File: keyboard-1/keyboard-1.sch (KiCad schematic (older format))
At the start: 14 parts

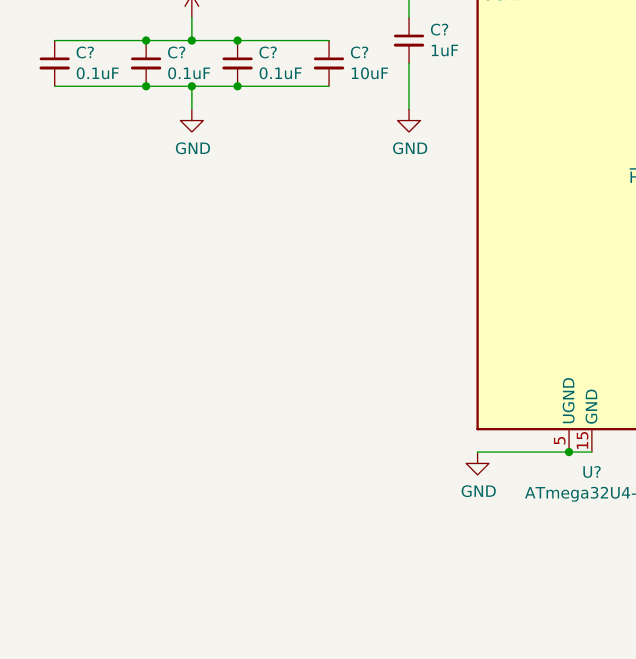
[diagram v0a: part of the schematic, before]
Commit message: mcu + usb-c connect
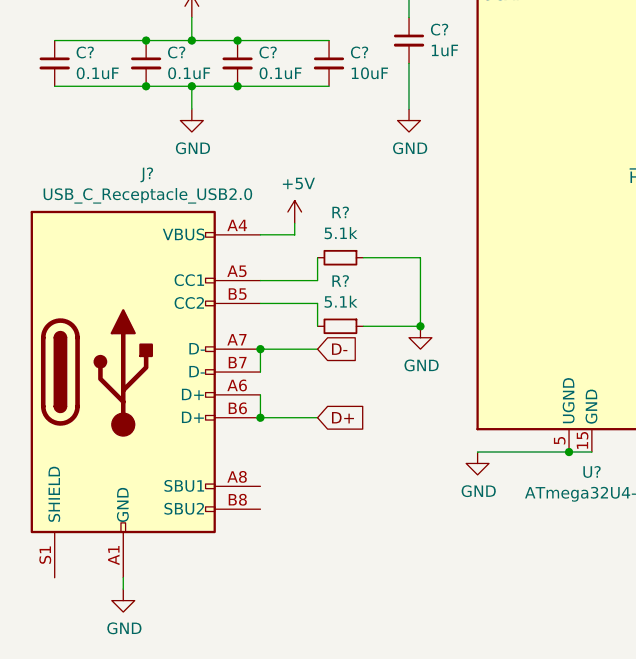
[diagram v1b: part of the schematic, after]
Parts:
- added J?: USB_C_Receptacle_USB2.0, symbol Connector:USB_C_Receptacle_USB2.0
- added R? (x2): 5.1k, symbol Device:R_Small
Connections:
- net +5V: now also J?.A4 (VBUS), J?.A9 (VBUS), J?.B4 (VBUS), J?.B9 (VBUS)
- net D+: now also J?.A6 (D+), J?.B6 (D+)
- net D-: now also J?.A7 (D-), J?.B7 (D-)
- net GND: now also J?.A1 (GND), J?.A12 (GND), J?.B1 (GND), J?.B12 (GND), R?.1, R?.1
- new net: J?.A5 (CC1), R?.2
- new net: J?.B5 (CC2), R?.2
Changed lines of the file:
@@
 Text GLabel 8350 3500 0    50   Input ~ 0
 D-
+$Comp
+L Connector:USB_C_Receptacle_USB2.0 J?
+U 1 1 601E80A6
+P 7750 5350
+F 0 "J?" H 7857 6217 50  0000 C CNN
+F 1 "USB_C_Receptacle_USB2.0" H 7857 6126 50  0000 C CNN
+F 2 "" H 7900 5350 50  0001 C CNN
+F 3 "https://www.usb.org/sites/default/files/documents/usb_type-c.zip" H 7900 5350 50  0001 C CNN
+	1    7750 5350
+	1    0    0    -1
+$EndComp
+$Comp
+L power:GND #PWR?
+U 1 1 601F3A88
+P 7750 6300
+F 0 "#PWR?" H 7750 6050 50  0001 C CNN
+F 1 "GND" H 7755 6127 50  0000 C CNN
+F 2 "" H 7750 6300 50  0001 C CNN
+F 3 "" H 7750 6300 50  0001 C CNN
+	1    7750 6300
+	1    0    0    -1
+$EndComp
+Wire Wire Line
+	7750 6250 7750 6300
+Text GLabel 8600 5550 2    50   Input ~ 0
+D+
+Text GLabel 8600 5250 2    50   Input ~ 0
+D-
+$Comp
+L power:+5V #PWR?
+U 1 1 601F53D3
+P 8500 4700
+F 0 "#PWR?" H 8500 4550 50  0001 C CNN
+F 1 "+5V" H 8515 4873 50  0000 C CNN
+F 2 "" H 8500 4700 50  0001 C CNN
+F 3 "" H 8500 4700 50  0001 C CNN
+	1    8500 4700
+	1    0    0    -1
+$EndComp
+Wire Wire Line
+	8350 4750 8500 4750
+Wire Wire Line
+	8500 4750 8500 4700
+Wire Wire Line
+	8350 5350 8350 5250
+Wire Wire Line
+	8350 5250 8600 5250
+Connection ~ 8350 5250
+Wire Wire Line
+	8350 5450 8350 5550
+Wire Wire Line
+	8350 5550 8600 5550
+Connection ~ 8350 5550
+$Comp
+L Device:R_Small R?
+U 1 1 601FA629
+P 8700 4850
+F 0 "R?" V 8504 4850 50  0000 C CNN
+F 1 "5.1k" V 8595 4850 50  0000 C CNN
+F 2 "" H 8700 4850 50  0001 C CNN
+F 3 "~" H 8700 4850 50  0001 C CNN
+	1    8700 4850
+	0    1    1    0
+$EndComp
+$Comp
+L Device:R_Small R?
+U 1 1 601FAF2C
+P 8700 5150
+F 0 "R?" V 8504 5150 50  0000 C CNN
+F 1 "5.1k" V 8595 5150 50  0000 C CNN
+F 2 "" H 8700 5150 50  0001 C CNN
+F 3 "~" H 8700 5150 50  0001 C CNN
+	1    8700 5150
+	0    1    1    0
+$EndComp
+$Comp
+L power:GND #PWR?
+U 1 1 601FB32C
+P 9050 5150
+F 0 "#PWR?" H 9050 4900 50  0001 C CNN
+F 1 "GND" H 9055 4977 50  0000 C CNN
+F 2 "" H 9050 5150 50  0001 C CNN
+F 3 "" H 9050 5150 50  0001 C CNN
+	1    9050 5150
+	1    0    0    -1
+$EndComp
+Wire Wire Line
+	8350 4950 8600 4950
+Wire Wire Line
+	8600 4950 8600 4850
+Wire Wire Line
+	8350 5050 8600 5050
+Wire Wire Line
+	8600 5050 8600 5150
+Wire Wire Line
+	8800 4850 9050 4850
+Wire Wire Line
+	9050 4850 9050 5150
+Wire Wire Line
+	8800 5150 9050 5150
+Connection ~ 9050 5150
 $EndSCHEMATC

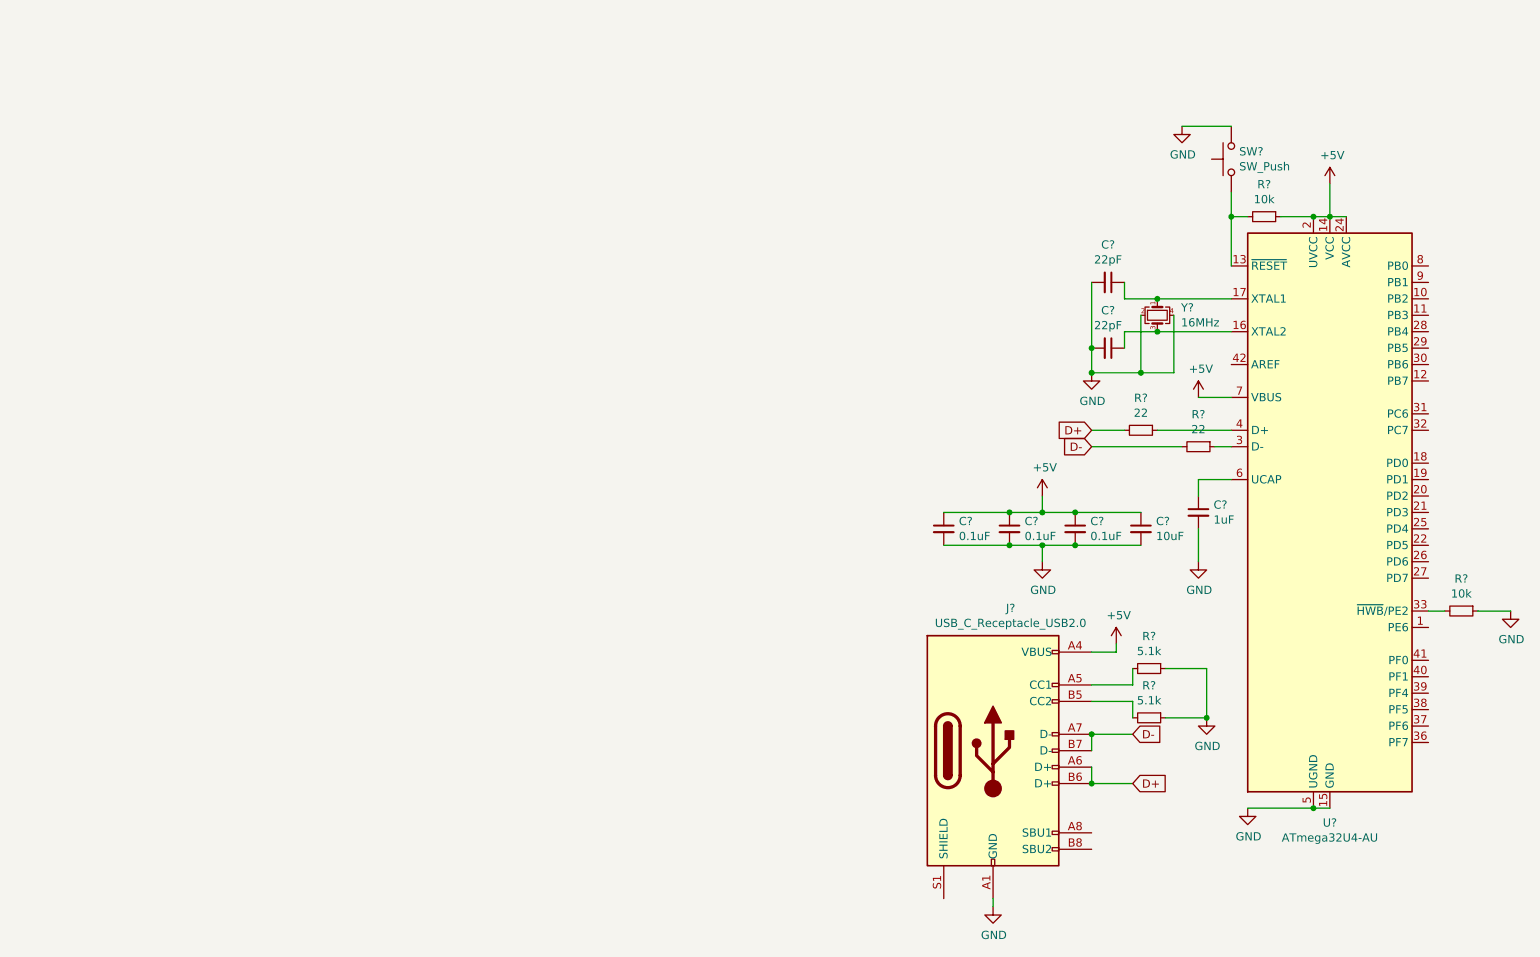
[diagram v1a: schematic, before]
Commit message: redo schematic, use double diodes, add column, use elite-c, start pcb design
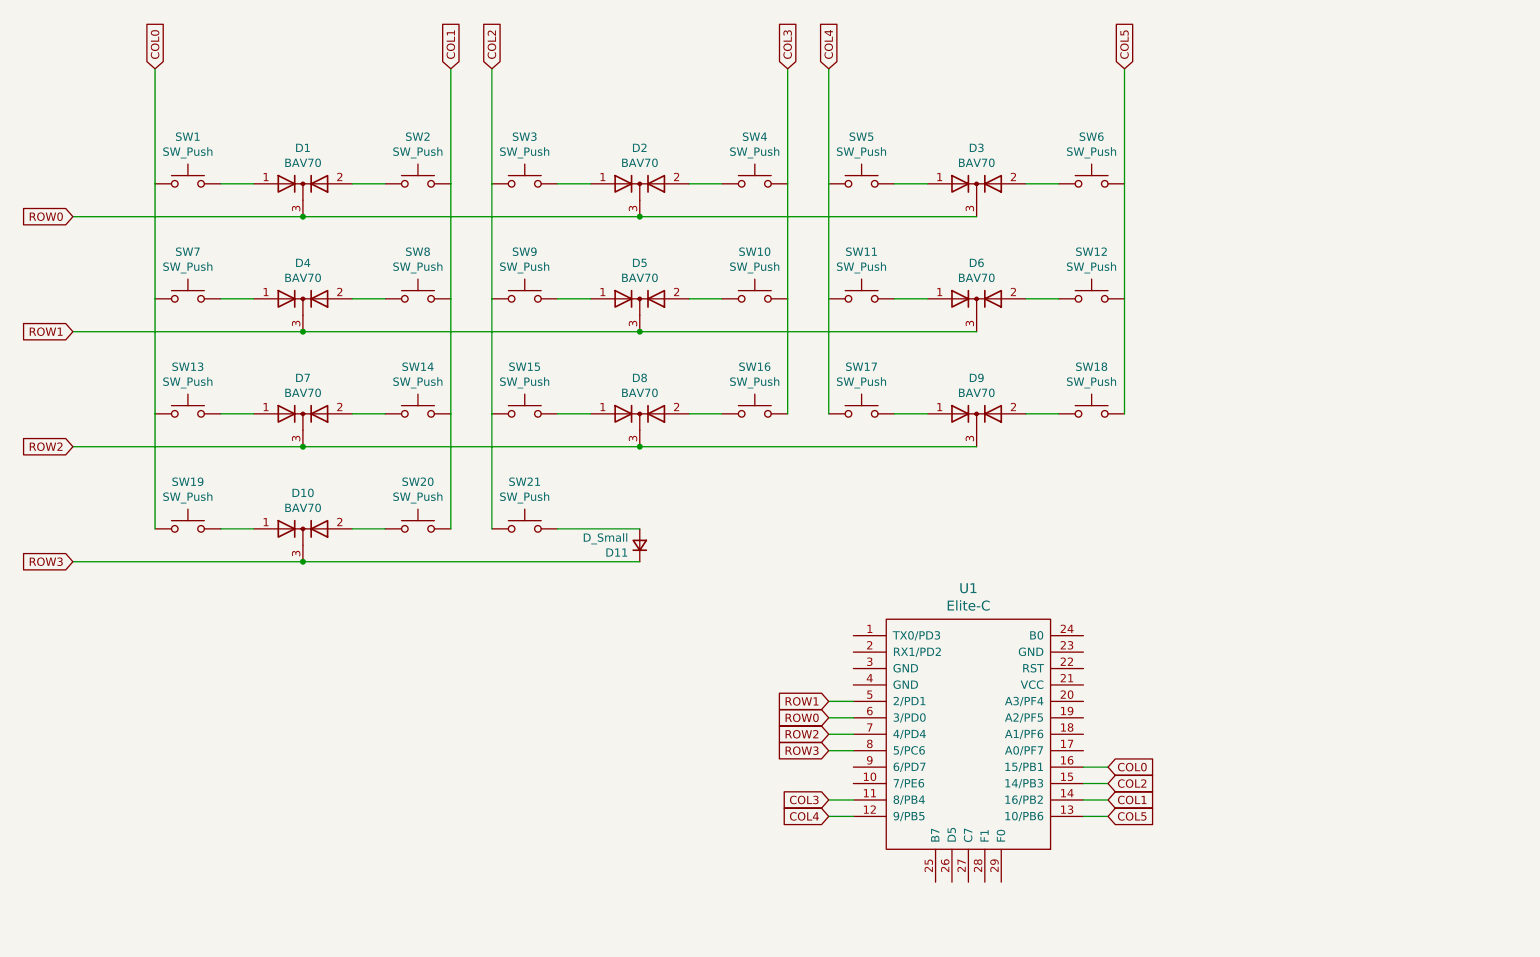
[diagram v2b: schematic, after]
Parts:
- removed C?: 1uF, symbol Device:C_Small
- removed C? (x3): 0.1uF, symbol Device:C_Small
- removed C?: 10uF, symbol Device:C_Small
- removed C? (x2): 22pF, symbol Device:C_Small
- removed J?: USB_C_Receptacle_USB2.0, symbol Connector:USB_C_Receptacle_USB2.0
- removed R? (x2): 10k, symbol Device:R_Small
- removed R? (x2): 22, symbol Device:R_Small
- removed R? (x2): 5.1k, symbol Device:R_Small
- removed SW?: SW_Push, symbol Switch:SW_Push
- removed U?: ATmega32U4-AU, Package_QFP:TQFP-44_10x10mm_P0.8mm, symbol MCU_Microchip_ATmega:ATmega32U4-AU
- removed Y?: 16MHz, symbol Device:Crystal_GND24_Small
- added D1, D10, D2, D3, D4, D5, D6, D7, D8, D9: BAV70, Package_TO_SOT_SMD:SOT-23, symbol Diode:BAV70
- added D11: D_Small, Diode_SMD:D_SOD-123, symbol Device:D_Small
- added SW1, SW10, SW11, SW12, SW13, SW14, SW15, SW16, SW17, SW18, SW19, SW2, SW20, SW21, SW3, SW4, SW5, SW6, SW7, SW8, SW9: SW_Push, Keebio-Parts:MX-Alps-Choc-1U, symbol Switch:SW_Push
- added U1: Elite-C, Keebio-Parts:Elite-C, symbol keebio:Elite-C
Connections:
- new net: D1.1 (A), SW1.2
- new net: D1.2 (A), SW2.1
- new net: D2.1 (A), SW3.2
- new net: D2.2 (A), SW4.1
- new net: D3.1 (A), SW5.2
- new net: D3.2 (A), SW6.1
- new net: D4.1 (A), SW7.2
- new net: D4.2 (A), SW8.1
- new net: D5.1 (A), SW9.2
- new net: D5.2 (A), SW10.1
- new net: D6.1 (A), SW11.2
- new net: D6.2 (A), SW12.1
- new net: D7.1 (A), SW13.2
- new net: D7.2 (A), SW14.1
- new net: D8.1 (A), SW15.2
- new net: D8.2 (A), SW16.1
- new net: D9.1 (A), SW17.2
- new net: D9.2 (A), SW18.1
- new net: D10.1 (A), SW19.2
- new net: D10.2 (A), SW20.1
- new net: D11.2 (A), SW21.2
- new net COL0: SW1.1, SW13.1, SW19.1, SW7.1, U1.16 (15/PB1)
- new net COL1: SW14.2, SW2.2, SW20.2, SW8.2, U1.14 (16/PB2)
- new net COL2: SW15.1, SW21.1, SW3.1, SW9.1, U1.15 (14/PB3)
- new net COL3: SW10.2, SW16.2, SW4.2, U1.11 (8/PB4)
- new net COL4: SW11.1, SW17.1, SW5.1, U1.12 (9/PB5)
- new net COL5: SW12.2, SW18.2, SW6.2, U1.13 (10/PB6)
- new net ROW0: D1.3 (K), D2.3 (K), D3.3 (K), U1.6 (3/PD0)
- new net ROW1: D4.3 (K), D5.3 (K), D6.3 (K), U1.5 (2/PD1)
- new net ROW2: D7.3 (K), D8.3 (K), D9.3 (K), U1.7 (4/PD4)
- new net ROW3: D10.3 (K), D11.1 (K), U1.8 (5/PC6)

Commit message: use generic connectors for elite C and add oled connectors, also add trrs connector
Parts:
- removed U1: Elite-C, Keebio-Parts:Elite-C, symbol keebio:Elite-C
- added J? (x2): Conn_01x12, symbol Connector_Generic:Conn_01x12
- added J?: Conn_01x04_Female, Connector_PinSocket_2.54mm:PinSocket_1x01_P2.54mm_Vertical, symbol Connector:Conn_01x04_Female
- added U2: TRRS, Keebio-Parts:TRRS-PJ-320A, symbol keebio:TRRS
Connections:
- net COL0: now also J?.4 (Pin_4)
- net COL1: now also J?.2 (Pin_2)
- net COL2: now also J?.3 (Pin_3)
- net COL3: now also J?.11 (Pin_11)
- net COL4: now also J?.12 (Pin_12)
- net COL5: now also J?.1 (Pin_1)
- net ROW0: now also J?.8 (Pin_8)
- net ROW1: now also J?.7 (Pin_7)
- net ROW2: now also J?.6 (Pin_6)
- net ROW3: now also J?.5 (Pin_5)
- new net GND: J?.11 (Pin_11), J?.4 (Pin_4), U2.1 (SLEEVE)
- new net SCL: J?.2 (Pin_2), J?.6 (Pin_6)
- new net SDA: J?.1 (Pin_1), J?.5 (Pin_5)
- new net SERIAL: J?.2 (Pin_2), U2.4 (RING2)
- new net VCC: J?.3 (Pin_3), J?.9 (Pin_9), U2.2 (TIP)
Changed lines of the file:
@@
 $EndDescr
-$Comp
-L keebio:Elite-C U1
-U 1 1 602DAF31
-P 7600 5200
-F 0 "U1" H 7600 6037 60  0000 C CNN
-F 1 "Elite-C" H 7600 5931 60  0000 C CNN
-F 2 "Keebio-Parts:Elite-C" V 8650 2700 60  0001 C CNN
-F 3 "" V 8650 2700 60  0001 C CNN
-	1    7600 5200
-	1    0    0    -1
-$EndComp
-Text GLabel 6750 1200 1    50   Input ~ 0
-COL4
-Text GLabel 6500 1200 1    50   Input ~ 0
-COL3
-Text GLabel 4700 1200 1    50   Input ~ 0
-COL2
-Text GLabel 4450 1200 1    50   Input ~ 0
-COL1
-Text GLabel 2650 1200 1    50   Input ~ 0
-COL0
-Text GLabel 6750 5350 0    50   Input ~ 0
-ROW3
-Text GLabel 2150 3500 0    50   Input ~ 0
-ROW2
-Text GLabel 2150 2800 0    50   Input ~ 0
-ROW1
-Text GLabel 2150 2100 0    50   Input ~ 0
-ROW0
 $Comp
 L Switch:SW_Push SW1
@@
 Wire Wire Line
 	7950 1900 8150 1900
-Text GLabel 8550 1200 1    50   Input ~ 0
-COL5
 Wire Wire Line
 	2150 2100 3550 2100
@@
 Wire Wire Line
 	5600 4000 5100 4000
-Text GLabel 6750 5150 0    50   Input ~ 0
+$Comp
+L keebio:TRRS U2
+U 1 1 603D1957
+P 5150 5300
+F 0 "U2" H 5067 5113 60  0000 C CNN
+F 1 "TRRS" H 5067 5219 60  0000 C CNN
+F 2 "Keebio-Parts:TRRS-PJ-320A" H 5300 5300 60  0001 C CNN
+F 3 "" H 5300 5300 60  0001 C CNN
+	1    5150 5300
+	-1   0    0    1
+$EndComp
+$Comp
+L power:VCC #PWR0103
+U 1 1 60418EEF
+P 5400 6000
+F 0 "#PWR0103" H 5400 5850 50  0001 C CNN
+F 1 "VCC" H 5415 6173 50  0000 C CNN
+F 2 "" H 5400 6000 50  0001 C CNN
+F 3 "" H 5400 6000 50  0001 C CNN
+	1    5400 6000
+	1    0    0    -1
+$EndComp
+$Comp
+L power:GND #PWR0104
+U 1 1 6041933E
+P 5650 5200
+F 0 "#PWR0104" H 5650 4950 50  0001 C CNN
+F 1 "GND" H 5655 5027 50  0000 C CNN
+F 2 "" H 5650 5200 50  0001 C CNN
+F 3 "" H 5650 5200 50  0001 C CNN
+	1    5650 5200
+	1    0    0    -1
+$EndComp
+Wire Wire Line
+	5500 5400 5500 5200
+Wire Wire Line
+	5500 5200 5650 5200
+Wire Wire Line
+	5500 5700 5500 6000
+Wire Wire Line
+	5500 6000 5400 6000
+$Comp
+L Connector_Generic:Conn_01x12 J?
+U 1 1 6044E7FE
+P 2450 5950
+F 0 "J?" H 2530 5942 50  0000 L CNN
+F 1 "Conn_01x12" H 2530 5851 50  0000 L CNN
+F 2 "" H 2450 5950 50  0001 C CNN
+F 3 "~" H 2450 5950 50  0001 C CNN
+	1    2450 5950
+	1    0    0    -1
+$EndComp
+$Comp
+L Connector_Generic:Conn_01x12 J?
+U 1 1 60456305
+P 3250 6050
+F 0 "J?" H 3168 5225 50  0000 C CNN
+F 1 "Conn_01x12" H 3168 5316 50  0000 C CNN
+F 2 "" H 3250 6050 50  0001 C CNN
+F 3 "~" H 3250 6050 50  0001 C CNN
+	1    3250 6050
+	-1   0    0    1
+$EndComp
+Wire Wire Line
+	3450 6050 3600 6050
+Wire Wire Line
+	3600 6150 3450 6150
+Wire Wire Line
+	3450 6250 3600 6250
+Wire Wire Line
+	3600 6350 3450 6350
+Wire Wire Line
+	3450 6450 3600 6450
+Wire Wire Line
+	3450 6550 3600 6550
+Wire Wire Line
+	3450 5850 3600 5850
+Wire Wire Line
+	3600 5950 3450 5950
+$Comp
+L Connector:Conn_01x04_Female J?
+U 1 1 60477B7D
+P 5350 7400
+F 0 "J?" V 5196 7548 50  0000 L CNN
+F 1 "Conn_01x04_Female" V 5287 7548 50  0000 L CNN
+F 2 "Connector_PinSocket_2.54mm:PinSocket_1x01_P2.54mm_Vertical" H 5350 7400 50  0001 C CNN
+F 3 "~" H 5350 7400 50  0001 C CNN
+	1    5350 7400
+	0    1    1    0
+$EndComp
+$Comp
+L power:VCC #PWR?
+U 1 1 60479E6C
+P 5250 6900
+F 0 "#PWR?" H 5250 6750 50  0001 C CNN
+F 1 "VCC" H 5265 7073 50  0000 C CNN
+F 2 "" H 5250 6900 50  0001 C CNN
+F 3 "" H 5250 6900 50  0001 C CNN
+	1    5250 6900
+	1    0    0    -1
+$EndComp
+$Comp
+L power:GND #PWR?
+U 1 1 6047AD0B
+P 4850 7200
+F 0 "#PWR?" H 4850 6950 50  0001 C CNN
+F 1 "GND" H 4855 7027 50  0000 C CNN
+F 2 "" H 4850 7200 50  0001 C CNN
+F 3 "" H 4850 7200 50  0001 C CNN
+	1    4850 7200
+	1    0    0    -1
+$EndComp
+Text Label 3600 5850 0    50   ~ 0
 ROW0
-Text GLabel 6750 5050 0    50   Input ~ 0
+Text Label 3600 5950 0    50   ~ 0
 ROW1
-Text GLabel 6750 5250 0    50   Input ~ 0
+Text Label 3600 6050 0    50   ~ 0
 ROW2
-Text GLabel 2150 4200 0    50   Input ~ 0
+Text Label 3600 6150 0    50   ~ 0
 ROW3
-Wire Wire Line
-	6750 5050 6900 5050
-Wire Wire Line
-	6900 5150 6750 5150
-Wire Wire Line
-	6900 5250 6750 5250
-Wire Wire Line
-	6750 5350 6900 5350
-Text GLabel 8450 5450 2    50   Input ~ 0
+Text Label 3600 6250 0    50   ~ 0
 COL0
-Text GLabel 8450 5650 2    50   Input ~ 0
+Text Label 3600 6350 0    50   ~ 0
+COL2
+Text Label 3600 6450 0    50   ~ 0
 COL1
-Text GLabel 8450 5550 2    50   Input ~ 0
+Text Label 3600 6550 0    50   ~ 0
+COL5
+Wire Wire Line
+	2100 6550 2250 6550
+Wire Wire Line
+	2250 6450 2100 6450
+Text Label 2100 6450 2    50   ~ 0
+COL3
+Text Label 2100 6550 2    50   ~ 0
+COL4
+$Comp
+L power:VCC #PWR?
+U 1 1 6048C43C
+P 4050 5650
+F 0 "#PWR?" H 4050 5500 50  0001 C CNN
+F 1 "VCC" H 4065 5823 50  0000 C CNN
+F 2 "" H 4050 5650 50  0001 C CNN
+F 3 "" H 4050 5650 50  0001 C CNN
+	1    4050 5650
+	1    0    0    -1
+$EndComp
+$Comp
+L power:GND #PWR?
+U 1 1 6048CE5C
+P 3800 5400
+F 0 "#PWR?" H 3800 5150 50  0001 C CNN
+F 1 "GND" H 3805 5227 50  0000 C CNN
+F 2 "" H 3800 5400 50  0001 C CNN
+F 3 "" H 3800 5400 50  0001 C CNN
+	1    3800 5400
+	1    0    0    -1
+$EndComp
+Wire Wire Line
+	3450 5750 4050 5750
+Wire Wire Line
+	4050 5750 4050 5650
+Wire Wire Line
+	3650 5400 3800 5400
+Wire Wire Line
+	3450 5550 3650 5550
+Wire Wire Line
+	3650 5550 3650 5400
+Text Label 5650 5500 0    50   ~ 0
+SERIAL
+Wire Wire Line
+	5500 5500 5650 5500
+Text Label 2100 5550 2    50   ~ 0
+SERIAL
+Wire Wire Line
+	2250 5550 2100 5550
+Text Label 2150 4200 2    50   ~ 0
+ROW3
+Text Label 2150 3500 2    50   ~ 0
+ROW2
+Text Label 2150 2800 2    50   ~ 0
+ROW1
+Text Label 2150 2100 2    50   ~ 0
+ROW0
+Text Label 2650 1200 1    50   ~ 0
+COL0
+Text Label 4450 1200 1    50   ~ 0
+COL1
+Text Label 4700 1200 1    50   ~ 0
 COL2
-Text GLabel 6750 5650 0    50   Input ~ 0
+Text Label 6500 1200 1    50   ~ 0
 COL3
-Text GLabel 6750 5750 0    50   Input ~ 0
+Text Label 6750 1200 1    50   ~ 0
 COL4
-Text GLabel 8450 5750 2    50   Input ~ 0
+Text Label 8550 1200 1    50   ~ 0
 COL5
-Wire Wire Line
-	8300 5450 8450 5450
-Wire Wire Line
-	8450 5550 8300 5550
-Wire Wire Line
-	8300 5650 8450 5650
-Wire Wire Line
-	8300 5750 8450 5750
-Wire Wire Line
-	6750 5750 6900 5750
-Wire Wire Line
-	6900 5650 6750 5650
+Text Label 2100 5950 2    50   ~ 0
+SCL
+Text Label 2100 5850 2    50   ~ 0
+SDA
+Wire Wire Line
+	2250 5850 2100 5850
+Wire Wire Line
+	2250 5950 2100 5950
+Wire Wire Line
+	5250 7200 5250 6900
+Wire Wire Line
+	5150 7200 4850 7200
+Text Label 5350 6950 0    50   ~ 0
+SCL
+Text Label 5450 7050 0    50   ~ 0
+SDA
+Wire Wire Line
+	5350 6950 5350 7200
+Wire Wire Line
+	5450 7050 5450 7200
 $EndSCHEMATC
